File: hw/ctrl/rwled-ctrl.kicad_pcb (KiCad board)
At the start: 2 copper layers, 70.9 x 38.1 mm, 55 parts, among them J21 batt-chg, J31 USB_B_Micro, J61 led-a, J62 led-b, J63 led-c, J64 led-d, J65 batt-ab, J66 batt-cd, Q31 UMH3N, Q51 ML2502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

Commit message: hw ctrl - плата доразведена
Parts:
- removed Q51, Q52: ML2502, Package_TO_SOT_SMD:SOT-23
- removed R52, R55, R63: 510, Resistor_SMD:R_0805_2012Metric
- removed R53, R56: 100k, Resistor_SMD:R_0805_2012Metric
- added Q64: UMH3N, Package_TO_SOT_SMD:SOT-363_SC-70-6, F.Cu at (155.6, 61.5)
- Q63: value c1815 -> UMH3N; footprint Package_TO_SOT_SMD:SOT-23 -> Package_TO_SOT_SMD:SOT-363_SC-70-6
- R11: moved to B.Cu
- U31: value CP2102 -> CP2104; footprint Package_DFN_QFN:QFN-28-1EP_5x5mm_P0.5mm_EP3.35x3.35mm -> Package_DFN_QFN:QFN-24-1EP_4x4mm_P0.5mm_EP2.6x2.6mm
- moved R11 25.6 mm to (136.8, 52.3), turned to -90 degrees
- moved C31 19.0 mm to (115.8, 51.6)
- moved D23 16.3 mm to (120.9, 50.7), turned to 180 degrees
- moved C61 15.3 mm to (116.7, 75.5), turned to -90 degrees
- moved R31 9.47 mm to (125.5, 44.6)
- moved R61 8.34 mm to (128.9, 58.0), turned to -90 degrees
- moved Q31 8.31 mm to (132.5, 52.6)
- moved R34 7.62 mm to (132.6, 45.6)
- moved C41 7.53 mm to (150.4, 55.7)
- moved U41 5.48 mm to (154.4, 55.7), turned to -90 degrees
- moved R51 5.30 mm to (160.6, 59.5), turned to 0 degrees
- moved D51 5.03 mm to (159.4, 63.0), turned to 0 degrees
- moved R13 4.99 mm to (123.7, 55.4), turned to -90 degrees
- moved D52 4.95 mm to (159.4, 55.6), turned to 0 degrees
- moved R54 4.61 mm to (160.6, 52.1), turned to 0 degrees
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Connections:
- C12 pad 1: GND -> /s-en
- C12 pad 2: /s-en -> GND
- Q62 pad 1: Net-(Q61-G) -> Net-(Q62-G)
- Q63 pad 1: Net-(Q63-B) -> Net-(Q61-G)
- Q63 pad 2: GND -> leden
- Q63 pad 3: Net-(Q61-G) -> Net-(Q62-G)
- R13 pad 1: /btn -> +3.3V
- R13 pad 2: +3.3V -> /btn
- R31 pad 1: VBUS -> Net-(U31-~{RST})
- R31 pad 2: Net-(U31-~{RST}) -> VBUS
- R32 pad 1: Net-(U31-TXD) -> /s-rx
- R32 pad 2: /s-rx -> Net-(U31-TXD)
- R33 pad 1: Net-(U31-RXD) -> /s-tx
- R33 pad 2: /s-tx -> Net-(U31-RXD)
- R34 pad 1: Net-(U31-SUSPEND) -> GND
- R34 pad 2: GND -> Net-(U31-SUSPEND)
- R62 pad 1: Net-(Q61-G) -> Net-(Q62-G)
- R64 pad 1: Net-(Q63-B) -> leden
- U11 pad 10: /ldata-a -> /ldata-c
- U11 pad 11: /ldata-b -> /ldata-a
- U11 pad 12: /ldata-c -> /ldata-b
- U31 pad 12: Net-(U31-SUSPEND) -> unconnected-(U31-RS485/GPIO.2-Pad12)
- U31 pad 17: unconnected-(U31-RS485/GPIO.2-Pad17) -> Net-(U31-SUSPEND)
- U31 pad 19: unconnected-(U31-~{TXT}/GPIO.0-Pad19) -> Net-(Q31A-E1)
- U31 pad 2: unconnected-(U31-~{RI}/CLK-Pad2) -> GND
- U31 pad 20: unconnected-(U31-GPIO.6-Pad20) -> Net-(U31-RXD)
- U31 pad 21: unconnected-(U31-GPIO.5-Pad21) -> Net-(U31-TXD)
- U31 pad 23: unconnected-(U31-~{CTS}-Pad23) -> Net-(Q31A-B1)
- U31 pad 24: Net-(Q31A-E1) -> unconnected-(U31-~{DCD}-Pad24)
- U31 pad 25: Net-(U31-RXD) -> GND
- U31 pad 3: GND -> Net-(J31-D+)
- U31 pad 4: Net-(J31-D+) -> Net-(J31-D-)
- U31 pad 5: Net-(J31-D-) -> Net-(U31-VDD)
- U31 pad 6: unconnected-(U31-VDD-Pad6) -> Net-(U31-VDD)
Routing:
- net +5V: track 0.00 -> 73.3 mm, vias 0 -> 2
- net /ldata-c: track 0.00 -> 61.4 mm
- net +3.3V: track 0.00 -> 50.5 mm, vias 0 -> 3
- net /ldata-d: track 0.00 -> 49.8 mm
- net /v-led-cd: track 0.00 -> 45.3 mm, vias 0 -> 6
- net GND: track 0.00 -> 41.0 mm, vias 0 -> 156
- net +BATT-CD: track 0.00 -> 39.7 mm
- net Net-(D24-A): track 0.00 -> 35.4 mm, vias 0 -> 12
- net /v-led-ab: track 0.00 -> 31.6 mm
- net +BATT-AB: track 0.00 -> 28.9 mm
- net /ldata-a: track 0.00 -> 24.9 mm
- net /s-boot: track 0.00 -> 24.2 mm, vias 0 -> 1
- net VBUS: track 0.00 -> 21.6 mm, vias 0 -> 1
- net /ldata-b: track 0.00 -> 21.2 mm
- net Net-(Q61-G): track 0.00 -> 19.0 mm
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- added copper zone on B.Cu, net GND
- added copper zone on F.Cu, net GND
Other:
- board text added: "+ D GND"
- board text added: "GND D +"

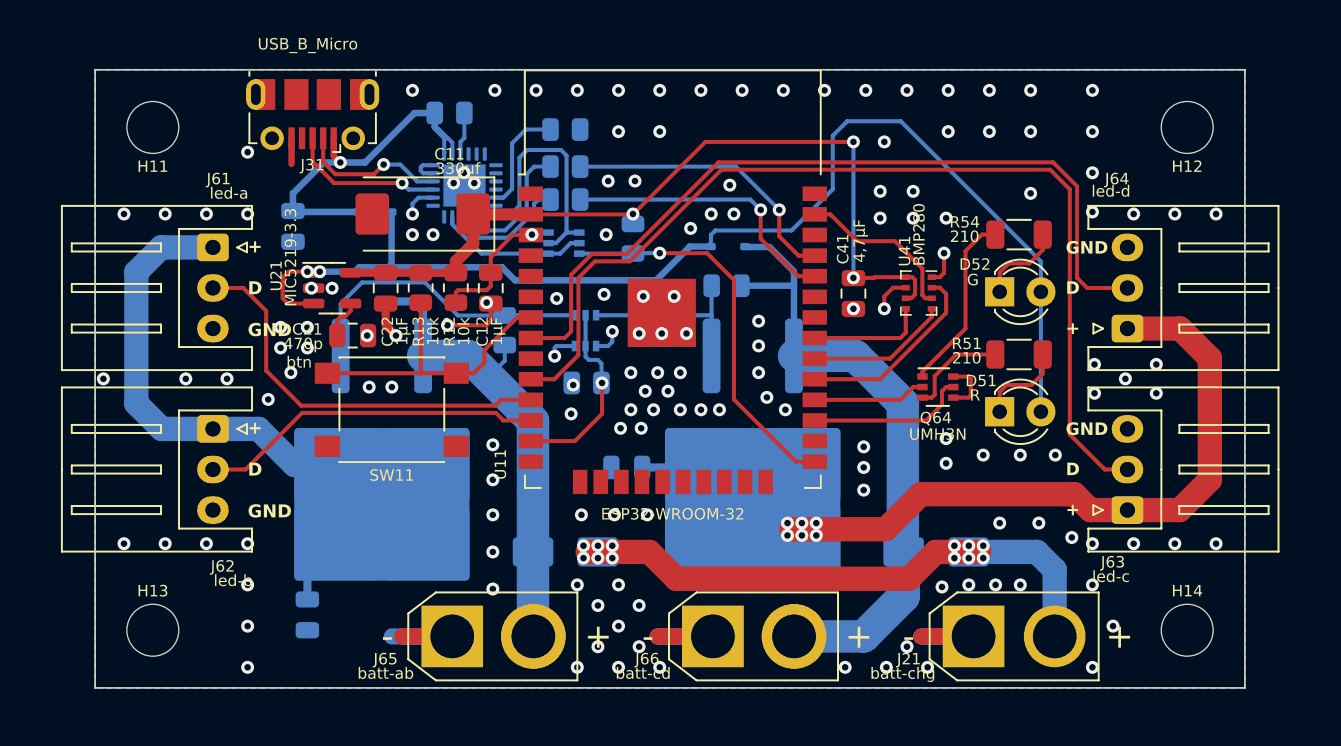
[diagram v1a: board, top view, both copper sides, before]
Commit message: hw led20 - перечерчен гербер
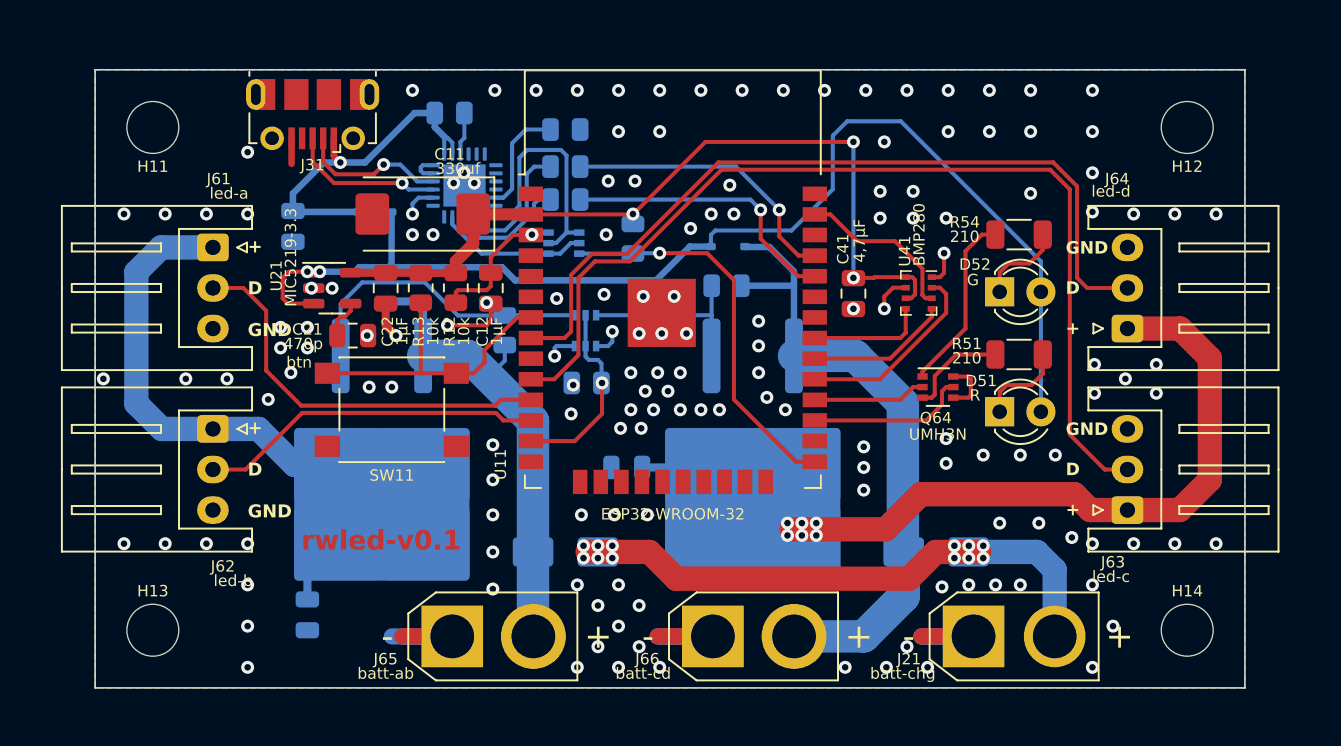
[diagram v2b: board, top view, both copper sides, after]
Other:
- board text added: "rwled-v0.1"
